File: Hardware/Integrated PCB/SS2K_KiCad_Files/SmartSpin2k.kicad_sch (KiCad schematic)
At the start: 88 parts, among them J1 B4B-XH-AMLFSN, J2 B8B-XH-A_LFSN, J3 10118194-0001LF, J4 B4B-XH-AMLFSN, Q1 S8050, Q2 S8050, Q3 S8050, Q4 S8050, SW1 SW_Push, SW4 SW_Push, U1 TMC2209-LA-T, U2 TPS5430DDA, U3 ESP32-WROOM-32D, U4 INTERFACE-CP2102-GMR(QFN28), U5 MAX3232, U6 LM1117-3.3

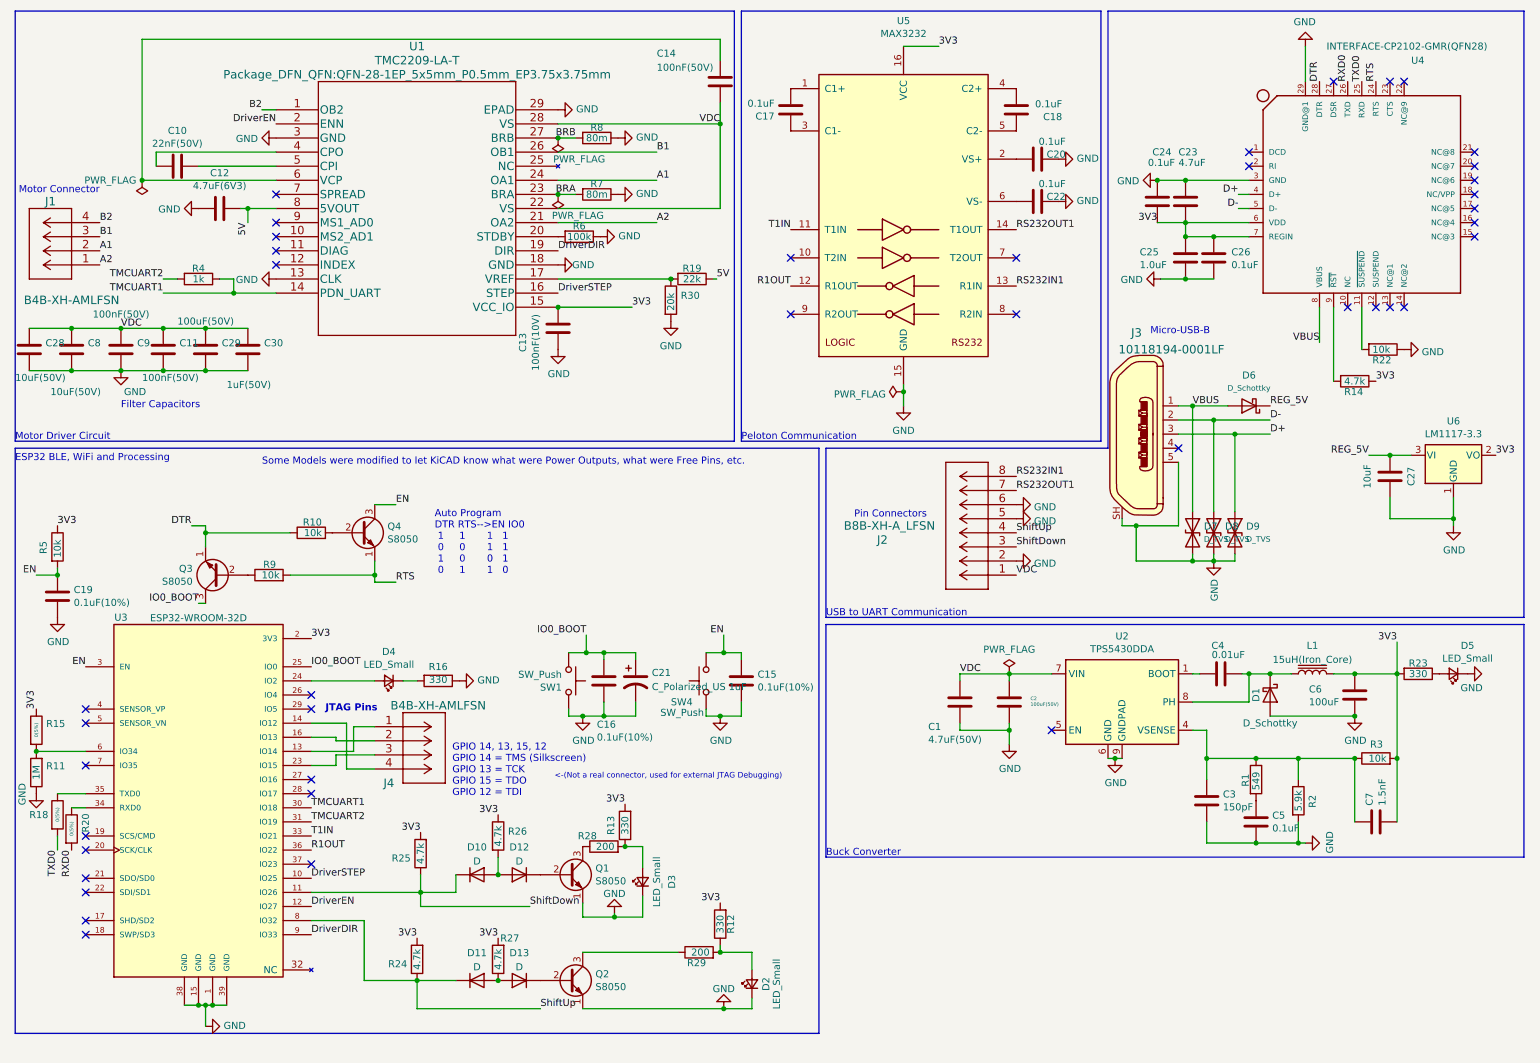
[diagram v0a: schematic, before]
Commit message: PCB Switch Added and LEDs moved
- Added SMD Switch near top of PCB to protrude outside of the case for Peloton bikes.
- Moved LEDs in order to allow for possible future "Light tubes" to show status of board outside of the case.
- Added Logos
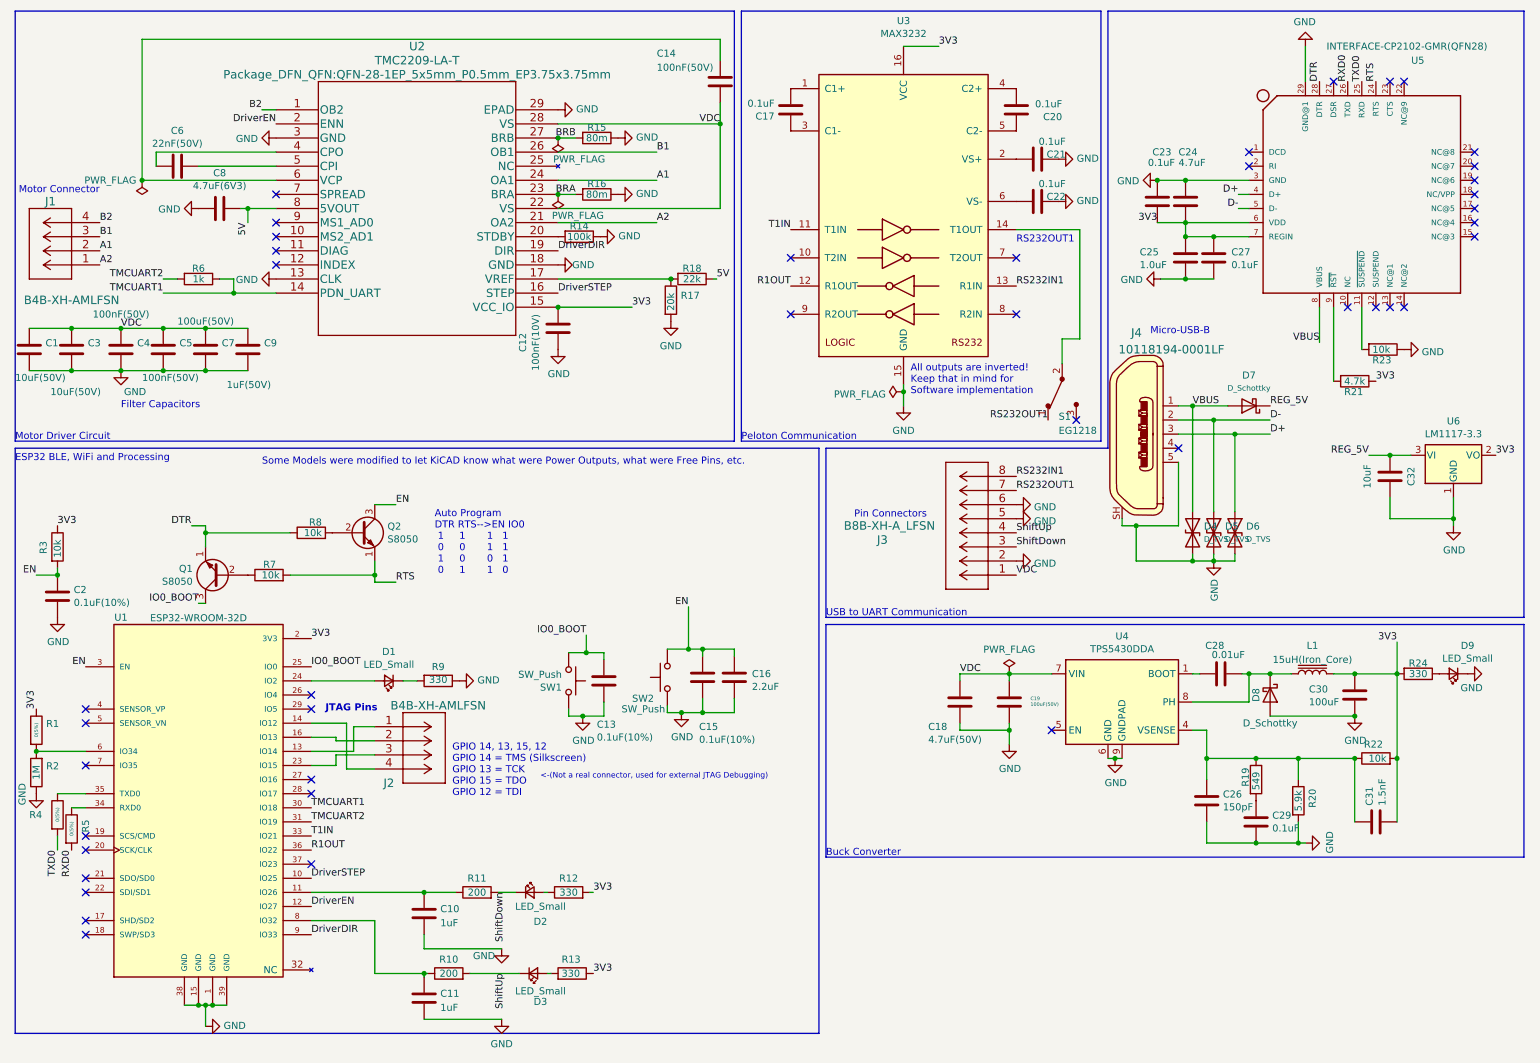
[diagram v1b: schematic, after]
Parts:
- removed C21: C_Polarized_US 1uF, Capacitor_SMD:C_0603_1608Metric, symbol Device:C_Polarized_US
- removed D10, D11, D12, D13: D, Diode_SMD:D_SOD-123F, symbol Device:D
- removed Q1, Q2: S8050, Package_TO_SOT_SMD:SOT-23, symbol Transistor_BJT:2N2219
- removed R12: 330, Resistor_SMD:R_0402_1005Metric, symbol Device:R
- removed R25, R26, R27: 4.7k, Resistor_SMD:R_0402_1005Metric, symbol Device:R
- removed R28, R29: 200, Resistor_SMD:R_0402_1005Metric, symbol Device:R
- added C10, C11: 1uF, Capacitor_SMD:C_0603_1608Metric, symbol Device:C
- added C16: 2.2uF, Capacitor_SMD:C_0402_1005Metric, symbol Device:C
- added R10, R11: 200, Resistor_SMD:R_0402_1005Metric, symbol Device:R
- added S1: EG1218, Button_Switch_SMD:SW_SPDT_PCM12, symbol dk_Slide-Switches:EG1218
- R13: renamed from R24; value 4.7k -> 330
- renumbered C28 to C1, C13 to C12, C16 to C13, C1 to C18, C2 to C19, C19 to C2, C18 to C20, C20 to C21, C24 to C23, C23 to C24, C3 to C26, C26 to C27, C4 to C28, C5 to C29, C8 to C3, C6 to C30, C7 to C31, C27 to C32, C9 to C4, C11 to C5, C10 to C6, C29 to C7, C12 to C8, C30 to C9, D4 to D1, D3 to D2, D2 to D3, D7 to D4, D8 to D5, D9 to D6, D6 to D7, D1 to D8, D5 to D9, J4 to J2, J2 to J3, J3 to J4, Q3 to Q1, Q4 to Q2, R15 to R1, R13 to R12, R6 to R14, R8 to R15, R7 to R16, R30 to R17, R19 to R18, R1 to R19, R11 to R2, R2 to R20, R14 to R21, R3 to R22, R22 to R23, R23 to R24, R5 to R3, R18 to R4, R20 to R5, R4 to R6, R9 to R7, R10 to R8, R16 to R9, SW4 to SW2, U3 to U1, U1 to U2, U5 to U3, U2 to U4, U4 to U5
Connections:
- net 3V3: now also R13.1; no longer R13.2
- net EN: now also C16.1
- net GND: now also C10.2, C11.2, C16.2; no longer D2.1 (K), D3.1 (K)
- net RS232OUT1: now also S1.1; no longer U3.14 (T1OUT)
- net ShiftDown: now also D2.1 (K), R11.2; no longer U1.11 (IO26)
- net ShiftUp: now also D3.1 (K), R10.2; no longer R13.1, U1.8 (IO32)
- net at D3.2 (A): now also R13.2
- new net: S1.2, U3.14 (T1OUT)
- new net: C10.1, R11.1, U1.11 (IO26)
- new net: C11.1, R10.1, U1.8 (IO32)
- no-connect marks 41 -> 42
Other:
- note added: "All outputs are inverted! Keep that in mind for Software implementation"
- note added: "RS232OUT1"
- moved on the sheet: C15, D2, D3, R12, R13, SW2
